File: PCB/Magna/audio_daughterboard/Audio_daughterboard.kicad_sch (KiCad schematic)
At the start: 33 parts, among them J101 Conn_02x15_Odd_Even, U202 CY2305SXC-1HT, U203 CY2305SXC-1HT

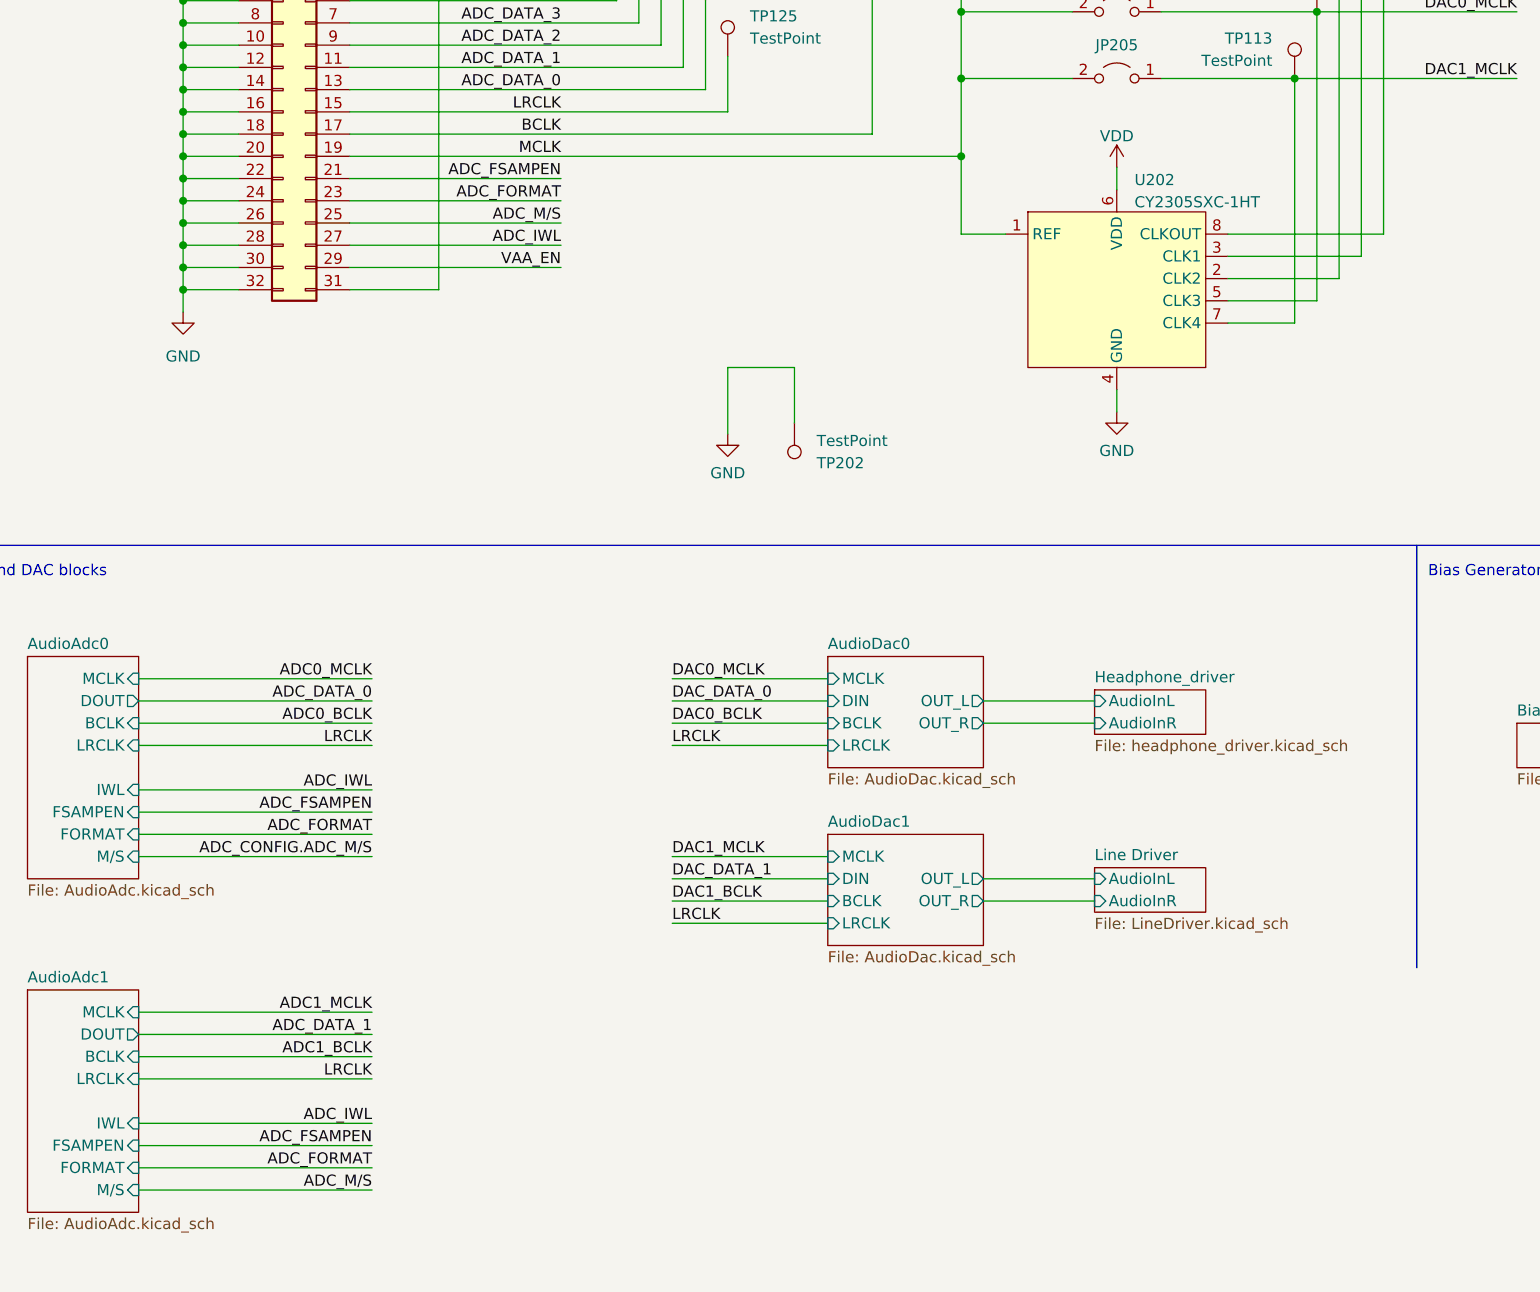
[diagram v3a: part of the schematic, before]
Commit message: Start of redesign of Audio board
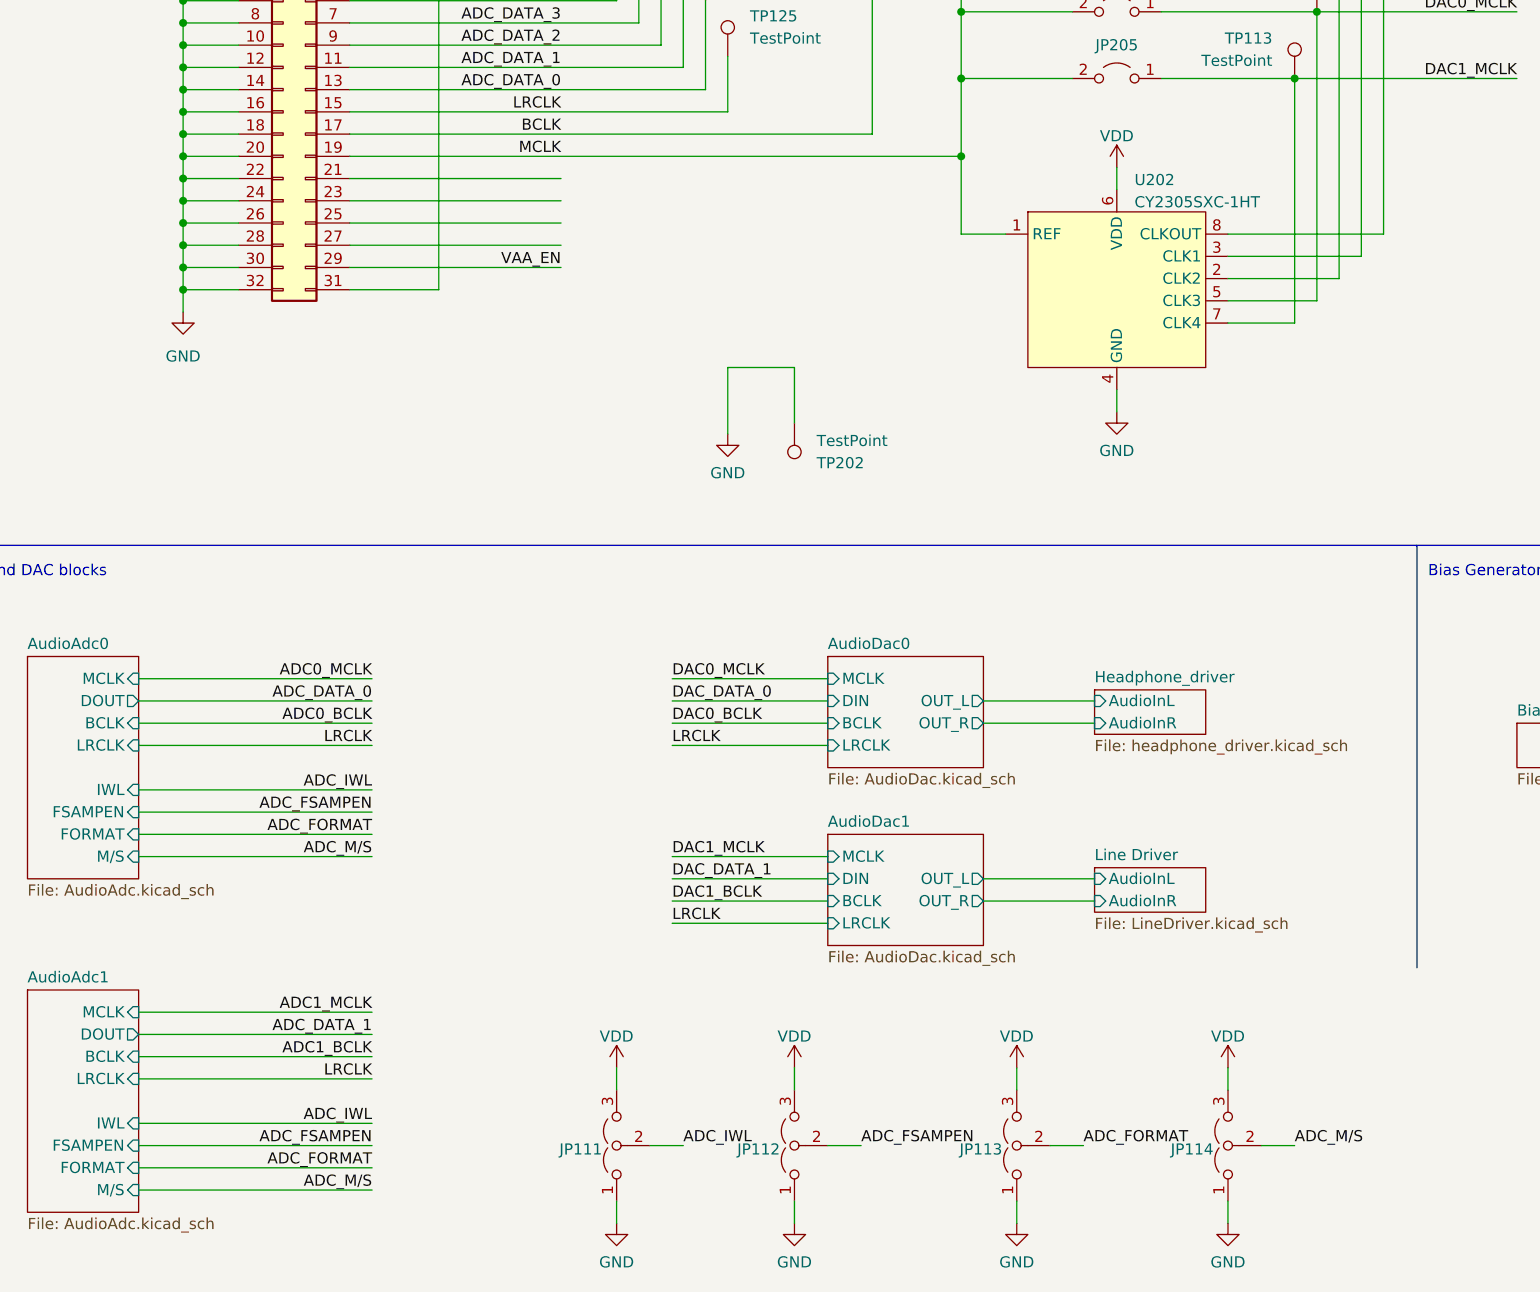
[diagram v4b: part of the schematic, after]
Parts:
- added JP111, JP112, JP113, JP114: SolderJumper_3_Bridged12, Jumper:SolderJumper-3_P2.0mm_Open_TrianglePad1.0x1.5mm_NumberLabels, symbol Jumper:Jumper_3_Open
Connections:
- net ADC_FORMAT: now also JP113.2 (C); no longer J101.23 (Pin_23)
- net ADC_FSAMPEN: now also JP112.2 (C); no longer J101.21 (Pin_21)
- net ADC_IWL: now also JP111.2 (C); no longer J101.27 (Pin_27)
- net ADC_M/S: now also JP114.2 (C); no longer J101.25 (Pin_25)
- net GND: now also JP111.1 (A), JP112.1 (A), JP113.1 (A), JP114.1 (A)
- net VDD: now also JP111.3 (B), JP112.3 (B), JP113.3 (B), JP114.3 (B)

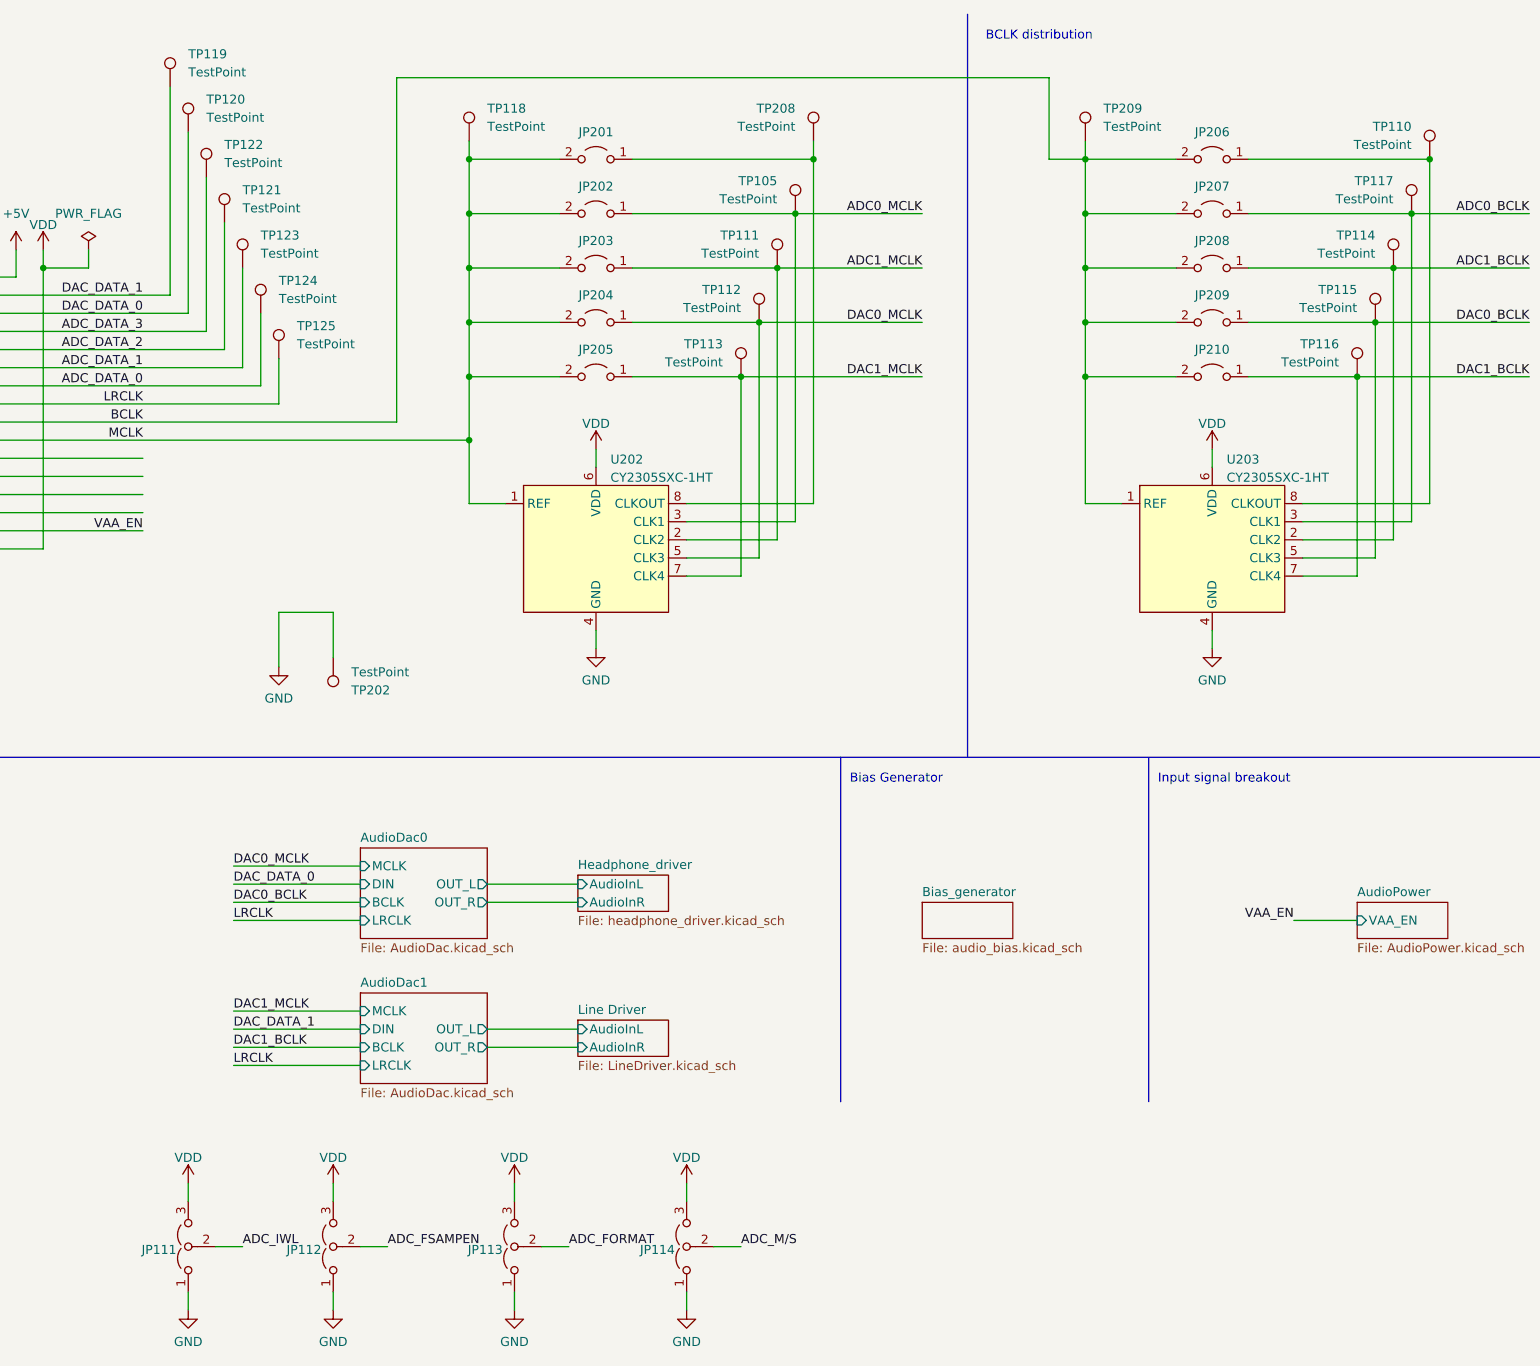
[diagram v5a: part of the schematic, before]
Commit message: Finish simulations and design of input filtering
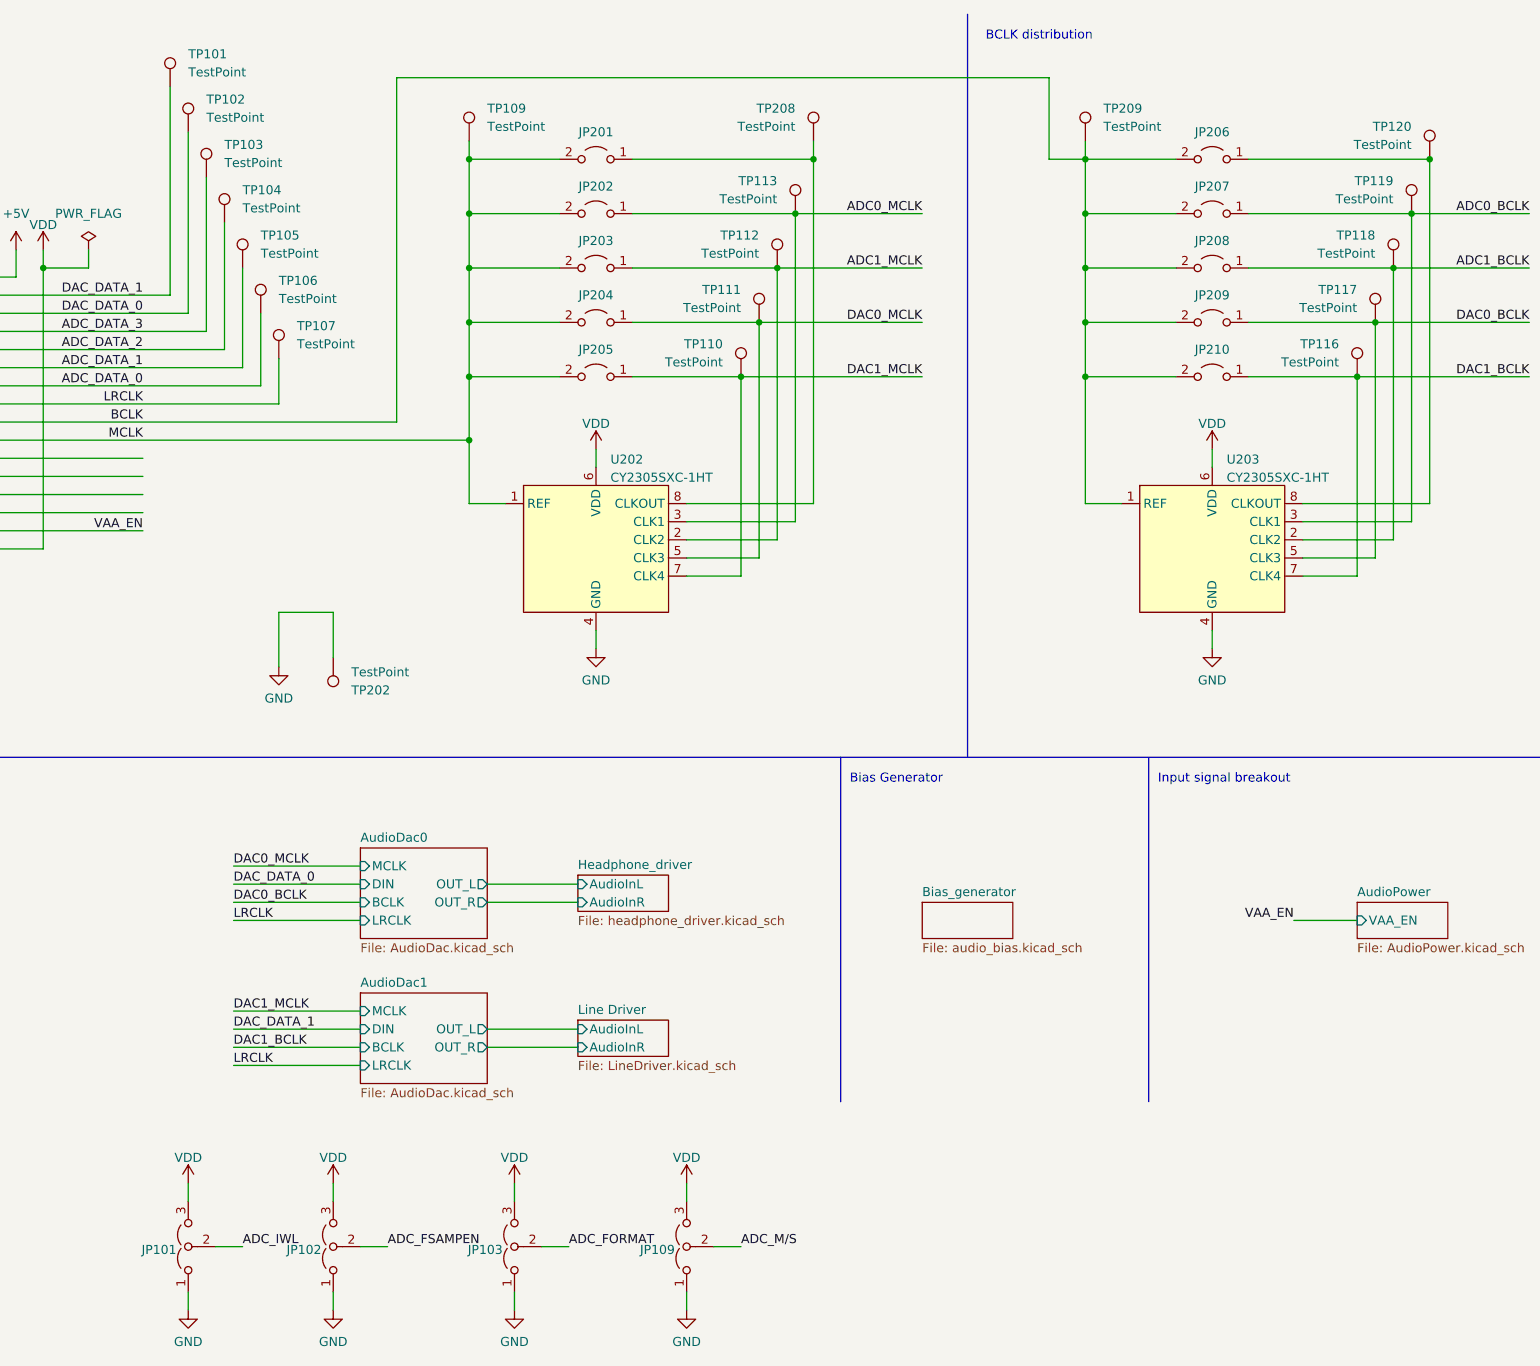
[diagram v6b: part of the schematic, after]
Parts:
- renumbered JP111 to JP101, JP112 to JP102, JP113 to JP103, JP114 to JP109, TP119 to TP101, TP120 to TP102, TP122 to TP103, TP121 to TP104, TP123 to TP105, TP124 to TP106, TP125 to TP107, TP118 to TP109, TP113 to TP110, TP112 to TP111, TP111 to TP112, TP105 to TP113, TP115 to TP117, TP114 to TP118, TP117 to TP119, TP110 to TP120

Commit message: Change ADC and add MCU for IO control
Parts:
- removed JP101, JP102, JP103, JP109: SolderJumper_3_Bridged12, Jumper:SolderJumper-3_P2.0mm_Open_TrianglePad1.0x1.5mm_NumberLabels, symbol Jumper:Jumper_3_Open
- removed JP201, JP202, JP203, JP204, JP205, JP206, JP207, JP208, JP209, JP210: Jumper_2_Open, Jumper:SolderJumper-2_P1.3mm_Open_TrianglePad1.0x1.5mm, symbol Jumper:Jumper_2_Open
- added JP104, JP105, JP106, JP107, JP115, JP116, JP117, JP118: Jumper_3_Bridged12, symbol Jumper:Jumper_3_Bridged12
- added R101, R102, R103, R104, R105, R106, R107, R108, R109, R110: R, symbol Device:R
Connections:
- net ADC0_BCLK: now also JP107.2 (C); no longer TP119.1, U203.3 (CLK1)
- net ADC0_MCLK: now also JP118.2 (C); no longer TP113.1, U202.3 (CLK1)
- net ADC1_BCLK: now also JP106.2 (C); no longer TP118.1, U203.2 (CLK2)
- net ADC1_MCLK: now also JP117.2 (C); no longer TP112.1, U202.2 (CLK2)
- net BCLK: now also TP116.1, TP117.1, TP118.1, TP119.1, JP104.3 (B), JP105.3 (B), JP106.3 (B), JP107.3 (B)
- net DAC0_BCLK: now also JP105.2 (C); no longer TP117.1, U203.5 (CLK3)
- net DAC0_MCLK: now also JP116.2 (C); no longer TP111.1, U202.5 (CLK3)
- net DAC1_BCLK: now also JP104.2 (C); no longer TP116.1, U203.7 (CLK4)
- net DAC1_MCLK: now also JP115.2 (C); no longer TP110.1, U202.7 (CLK4)
- net GND: now also R102.2, R104.2, R106.2, R108.2, R110.2
- net MCLK: now also TP110.1, TP111.1, TP112.1, TP113.1, JP115.3 (B), JP116.3 (B), JP117.3 (B), JP118.3 (B)
- net VDD: now also R101.1, R103.1, R105.1, R107.1, R109.1
- net CFG_SPI_CLK: now reaches J101.21 (Pin_21)
- net CFG_SPI_MISO: now reaches J101.23 (Pin_23)
- net CFG_SPI_MOSI: now reaches J101.25 (Pin_25)
- net CFG_SPI_NCS: now reaches J101.27 (Pin_27)
- new net: JP106.1 (A), U203.2 (CLK2)
- new net: JP107.1 (A), U203.3 (CLK1)
- new net: JP105.1 (A), U203.5 (CLK3)
- new net: JP104.1 (A), U203.7 (CLK4)
- new net: JP115.1 (A), U202.7 (CLK4)
- new net: JP117.1 (A), U202.2 (CLK2)
- new net: JP116.1 (A), U202.5 (CLK3)
- new net: JP118.1 (A), U202.3 (CLK1)
- new net AudioDac0/ADR5/ADR1/RSV: R109.2, R110.1
- new net AudioDac0/MODE: R101.2, R102.1
- new net AudioDac0/MS/ADR0/RSV: R107.2, R108.1
- new net AudioDac1/ADR5/ADR1/RSV: R105.2, R106.1
- new net AudioDac1/MS/ADR0/RSV: R103.2, R104.1
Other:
- added sheet Config MCU (Config_MCU.kicad_sch)
- sheet AudioAdc0 ports: added AMP_CLK, AMP_DATA, AMP_LOAD; removed none
- sheet AudioAdc1 ports: added AMP_CLK, AMP_DATA, AMP_LOAD; removed none
- sheet AudioDac0 ports: added ADR5/ADR1/RSV, MC/SCL/DMT, MD/SDA/DEMP, MODE, MS/ADR0/RSV, MUTE, ~{RST}; removed none
- sheet AudioDac1 ports: added ADR5/ADR1/RSV, MC/SCL/DMT, MD/SDA/DEMP, MODE, MS/ADR0/RSV, MUTE, ZERO1, ZERO2, ~{RST}; removed none
- note added: "MCLK distribution"
- moved on the sheet: TP109, TP110, TP111, TP112, TP113, TP208, TP209, U202, U203

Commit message: Some updates to PCB
Honestly I cannot remember whats changed
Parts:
- renumbered TP202 to TP108, TP208 to TP114, TP209 to TP115, U202 to U101, U203 to U102
